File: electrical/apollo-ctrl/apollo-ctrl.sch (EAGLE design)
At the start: 24 parts, among them J1 BARREL-JACK, Q1 N-chan, U1 NANO

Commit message: DIY version of PCB sort of done, require review
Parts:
- removed J1: BARREL-JACK, apollo-ctrl:POWER_JACKPTH
- added BAT1: (no value), apollo-ctrl:BATTERYAA-KIT
- added C1: 47u or more, apollo-ctrl:CAP_POLPTH4
- added C2: 100n, apollo-ctrl:CAPPTH
- added COIL2: (no value), apollo-ctrl:M023.5MM
- added D10, D11, D12: 3V6, apollo-ctrl:DIODE-ZENER1N4148
- added D4, D5: DIODE-SCHOTTKYPTH, apollo-ctrl:DIODE-SCHOTTKYPTH
- added D6, D7, D8, D9: (no value), apollo-ctrl:DIODE1N4148
- added F3: PTC, apollo-ctrl:PTCPTH
- added JP7, JP8: STAND-OFF, apollo-ctrl:STAND-OFF
- added LOGO1: APOLLO-LOGO, apollo-ctrl:APOLLO-LOGO
- added OK2: PC817, apollo-ctrl:PC817
- added Q2: N-chan, apollo-ctrl:MOSFET-NCHANNELPTH2
- added R10, R11, R12, R13, R14, R15, R7, R8: 620R, apollo-ctrl:RESISTORPTH-1/4W
- added R6, R9: 10K, apollo-ctrl:RESISTORPTH-1/4W
- added S1: (no value), apollo-ctrl:TAC_SWITCHPTH
- added TVS3, TVS4, TVS5, TVS6, TVS7: TVS 16V, apollo-ctrl:TVS1N4148
- added U2: HONEYWELL-MPR, apollo-ctrl:HONEYWELL-MPR-GAGE-DIY
- added X1: BARREL-JACK, apollo-ctrl:POWER_JACKPTH
- added X2: SENSOR-O2, apollo-ctrl:SENSOR-O2-JST-VERT
- added X3: (no value), apollo-ctrl:M05PTH
- D1: value (none) -> 3V6; device apollo-ctrl:DIODE1N4148 -> apollo-ctrl:DIODE-ZENER1N4148
- D2: value (none) -> DIODE-SCHOTTKYPTH; device apollo-ctrl:DIODE1N4148 -> apollo-ctrl:DIODE-SCHOTTKYPTH
- F1: value PTC -> FUSE 3A; device apollo-ctrl:PTCPTH -> apollo-ctrl:FUSE-4PIN-KEYSTONE-3568; SKU RHEF070HF-ND -> (none)
- F2: value FUSE 3A -> PTC; device apollo-ctrl:FUSE-4PIN-KEYSTONE-3568 -> apollo-ctrl:PTCPTH; SKU (none) -> RHEF070HF-ND
- LED1: value (none) -> GRN
- LED2: value (none) -> RED
- R1: value 1K -> 470R 500mW; device apollo-ctrl:RESISTORPTH-1/4W -> apollo-ctrl:RESISTORPTH-1/2W
- R5: value 1K -> 4K7
- SG1: value BUZZER-POL-AI-3035 -> BUZZER
- TVS1: device apollo-ctrl:TVS -> apollo-ctrl:TVS1N4148; SKU P6KE16CALFCT-ND -> (none)
- TVS2: value TVS -> TVS 16V; device apollo-ctrl:TVS -> apollo-ctrl:TVS1N4148; SKU (none) -> P6KE16CALFCT-ND
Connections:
- removed net N$1: COIL1.2, D1.C, TVS2.2
- new net 3.3V: C2.1, R4.2, R5.2, U1.3.3V, U2.VDD
- new net 5V: D4.C, U1.5V, X2.VCC, X3.5
- new net AUX: U1.D12/MOSI, X3.2
- new net BUTTON: S1.1, S1.2, TVS5.C, U1.D11/MISO
- new net BUZZ: SG1.P, U1.D8/ICP1
- new net COIL-2: R10.1, R9.2, U1.D6/OC0A
- new net COIL-2-CHECK: OK2.COL, U1.D7
- new net LED-G: R12.2, U1.D10/OC1B
- new net LED-R: R13.2, U1.D9/OC1A
- new net MCU-TO-O2: R14.2, U1.D3/INT1/OC2B
- new net N$10: COIL2.1, D8.A, D9.A, F3.2, TVS4.C
- new net N$11: F3.1, Q2.D
- new net N$12: D9.C, R11.1
- new net N$13: D3.C, D5.A, F1.2A, F1.2B, R2.2
- new net N$14: BAT1.+, D2.C, D4.A
- new net N$15: LED2.A, R13.1
- new net N$16: LED1.A, R12.1
- new net N$17: R14.1, TVS6.C, X2.RX
- new net N$18: R15.1, TVS7.C, X2.TX
- new net N$19: D1.C, D2.A, R1.1
- new net N$8: OK2.A, R11.2
- new net N$9: Q2.G, R10.2
- new net O2-TO-MCU: R15.2, U1.D2/INT0
- new net SCL: D10.C, R4.1, U1.A5/SCL, U2.SCLK/SCL, X3.4
- new net SDA: D11.C, R5.1, U1.A4/SDA, U2.MOSI/SDA, X3.3
- net +12V: now also C1.+, COIL1.2, COIL2.2, D5.C, D6.C, D8.C, R1.2, TVS1.C, TVS3.C, U1.VBAT; no longer D3.C, F2.2A, F2.2B, R4.2
- net COIL-1: now also R6.2, R7.1, U1.D4; no longer R1.1, R2.2
- net COIL-1-CHECK: now also U1.D5/OC0B
- net GND: now also BAT1.-, C1.-, C2.2, D1.A, D10.A, D11.A, D12.A, LED1.C, LED2.C, OK2.C, OK2.EMIT, Q2.S, R3.1, R6.1, R9.1, S1.3, S1.4, SG1.N, TVS1.A, TVS2.A, TVS3.A, TVS4.A, TVS5.A, TVS6.A, TVS7.A, U1.GND, U1.GND2, U2.VSS, X1.GND, X1.GNDBREAK, X2.GND, X3.1; no longer J1.GND, J1.GNDBREAK, R2.1, R5.1, TVS1.1, TVS2.1
- net N$2: now also F2.1; no longer F1.1
- net N$3: now also R7.2; no longer R1.2
- net N$4: now also R8.2; no longer R3.2
- net N$5: now also D6.A, D7.A, F2.2, TVS2.C; no longer D1.A, D2.A, F1.2, TVS1.2
- net N$6: now also F1.1A, F1.1B, X1.PWR; no longer F2.1A, F2.1B, J1.PWR
- net N$7: now also D7.C, R8.1; no longer D2.C, R3.1
- net V-MON: now also D12.C, R2.1, R3.2, U1.A3; no longer R4.1, R5.2
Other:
- note added: "backup power diode-OR"
- note added: "continuity checker"
- note added: "detects if coil is open or fuse is blown"
- note added: "flyback"
- note added: "over-voltage and reverse polarity protection"
- note added: "poor-man's battery charger treats the battery like a super-cap use Li-Ion only! 14400 cell"
- note added: "power fail detection"
- moved on the sheet: COIL1, D3, F1, F2, LED1, LED2, OK1, Q1, R1, R2, R3, R4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

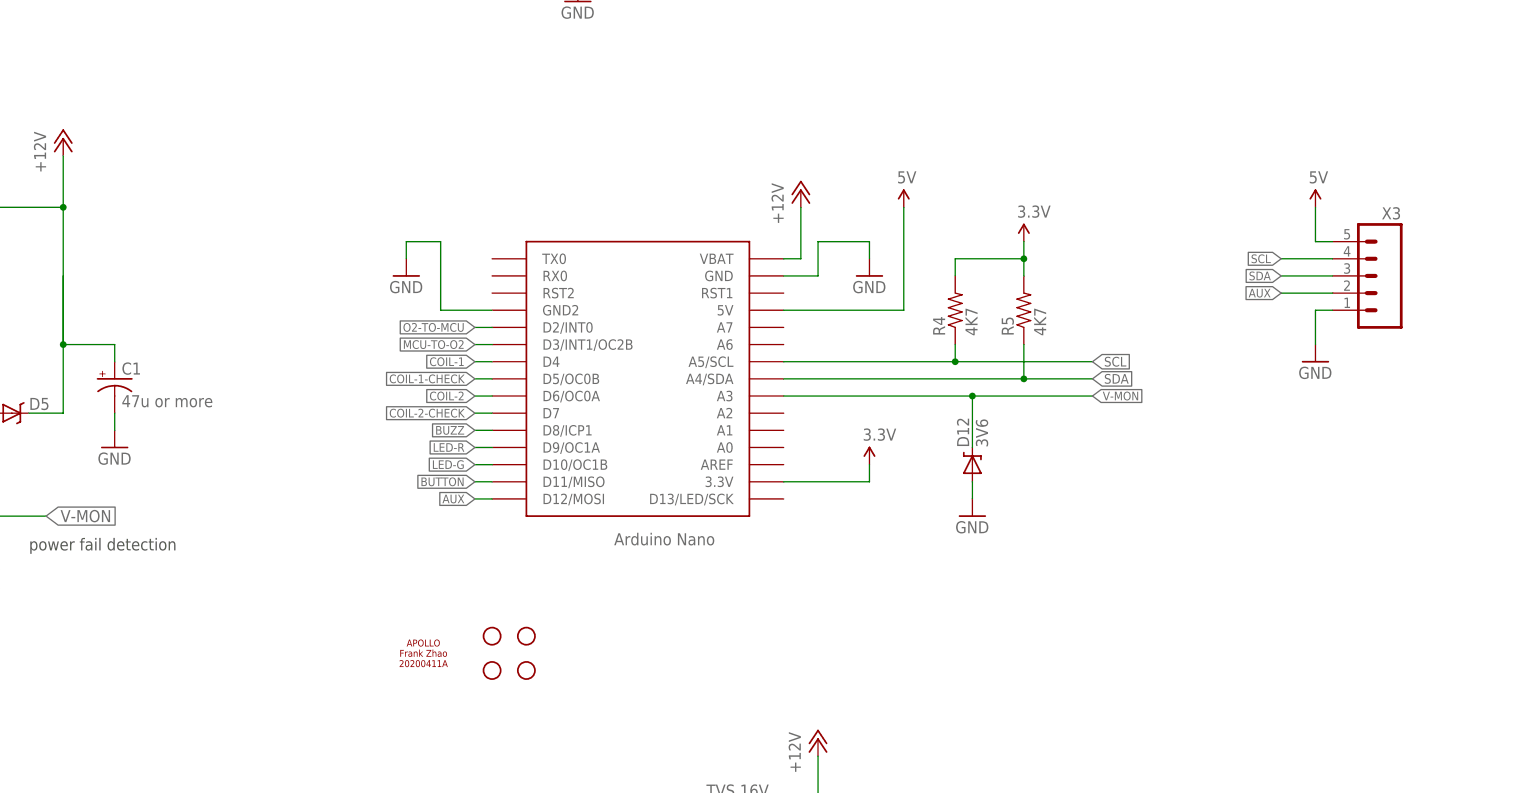
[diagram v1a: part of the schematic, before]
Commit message: added more spare pins to i2c header
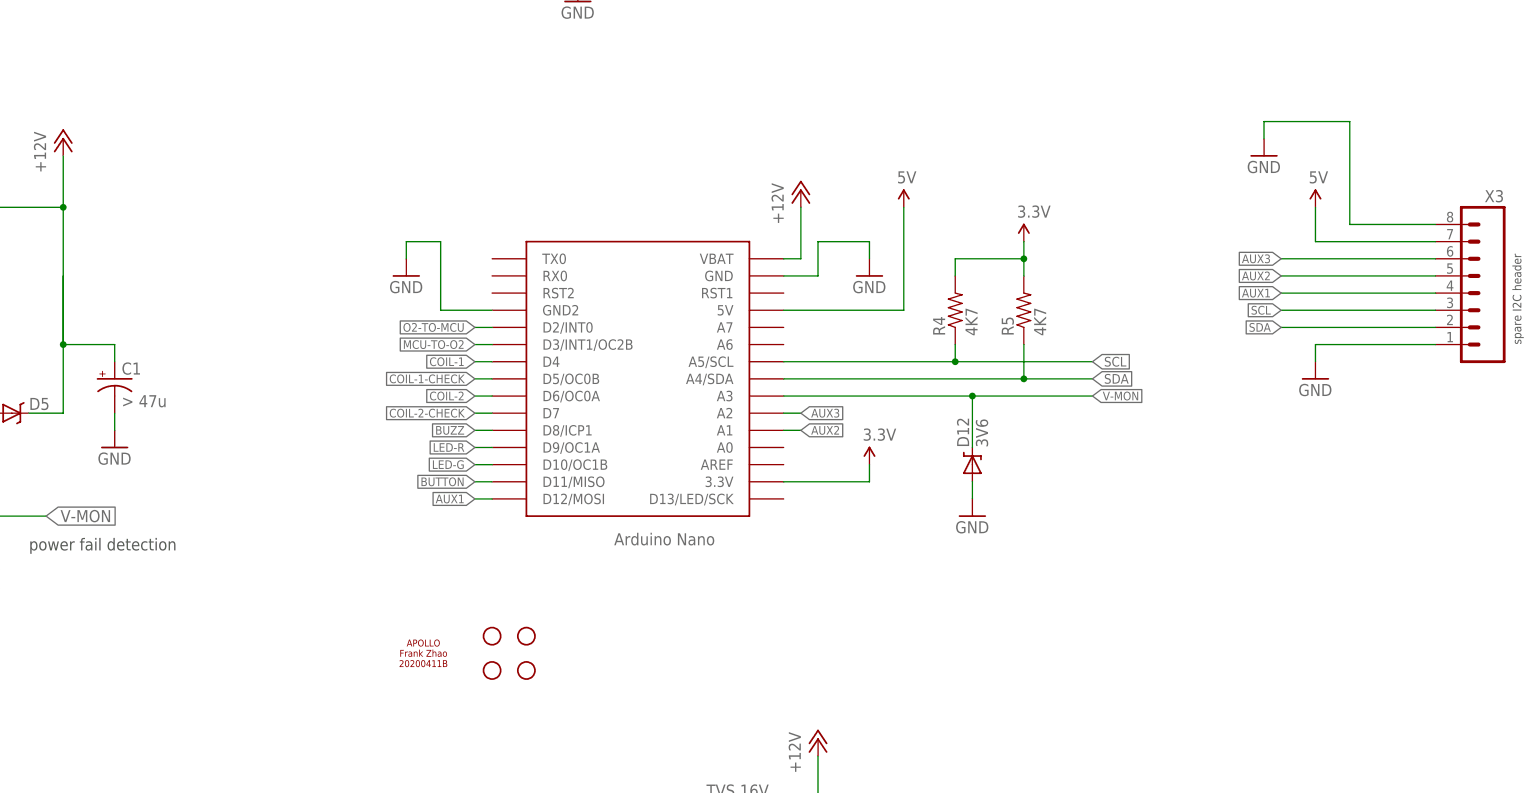
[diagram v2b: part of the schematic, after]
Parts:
- C1: value 47u or more -> > 47u
- X3: device apollo-ctrl:M05PTH -> apollo-ctrl:M081X08
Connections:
- removed net AUX: U1.D12/MOSI, X3.2
- new net AUX1: U1.D12/MOSI, X3.4
- new net AUX2: U1.A1, X3.5
- new net AUX3: U1.A2, X3.6
- net 5V: now also X3.7; no longer X3.5
- net GND: now also X3.8
- net SCL: now also X3.3; no longer X3.4
- net SDA: now also X3.2; no longer X3.3
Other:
- note added: "spare I2C header"
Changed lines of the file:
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@@
 <part name="C2" library="apollo-ctrl" deviceset="CAP" device="PTH" value="100n"/>
 <part name="GND5" library="apollo-ctrl" deviceset="GND" device=""/>
-<part name="C1" library="apollo-ctrl" deviceset="CAP_POL" device="PTH4" value="47u or more"/>
+<part name="C1" library="apollo-ctrl" deviceset="CAP_POL" device="PTH4" value="&gt; 47u"/>
 <part name="X2" library="apollo-ctrl" deviceset="SENSOR-O2" device="-JST-VERT" value="SENSOR-O2"/>
 <part name="GND26" library="apollo-ctrl" deviceset="GND" device=""/>
@@
 <part name="GND29" library="apollo-ctrl" deviceset="GND" device=""/>
 <part name="P+10" library="apollo-ctrl" deviceset="5V" device=""/>
-<part name="X3" library="apollo-ctrl" deviceset="M05" device="PTH"/>
 <part name="GND30" library="apollo-ctrl" deviceset="GND" device=""/>
 <part name="P+11" library="apollo-ctrl" deviceset="5V" device=""/>
+<part name="GND31" library="apollo-ctrl" deviceset="GND" device=""/>
+<part name="X3" library="apollo-ctrl" deviceset="M08" device="1X08"/>
 </parts>
 <sheets>
@@
 coil is open
 or fuse is blown</text>
+<text x="162.56" y="45.72" size="1.27" layer="97" rot="R90">spare I2C header</text>
 </plain>
 <instances>
@@
 <attribute name="VALUE" x="-87.376" y="56.896" size="1.778" layer="96"/>
 </instance>
-<instance part="X3" gate="G$1" x="142.24" y="55.88" rot="MR0"/>
-<instance part="GND30" gate="1" x="132.08" y="43.18" smashed="yes">
-<attribute name="VALUE" x="129.54" y="40.64" size="1.778" layer="96"/>
+<instance part="GND30" gate="1" x="132.08" y="40.64" smashed="yes">
+<attribute name="VALUE" x="129.54" y="38.1" size="1.778" layer="96"/>
 </instance>
 <instance part="P+11" gate="G$1" x="132.08" y="66.04" smashed="yes">
 <attribute name="VALUE" x="131.064" y="69.596" size="1.778" layer="96"/>
 </instance>
+<instance part="GND31" gate="1" x="124.46" y="73.66" smashed="yes">
+<attribute name="VALUE" x="121.92" y="71.12" size="1.778" layer="96"/>
+</instance>
+<instance part="X3" gate="G$1" x="154.94" y="53.34" rot="MR0"/>
 </instances>
 <busses>
@@
 <segment>
 <pinref part="GND30" gate="1" pin="GND"/>
-<wire x1="132.08" y1="45.72" x2="132.08" y2="50.8" width="0.1524" layer="91"/>
+<wire x1="132.08" y1="45.72" x2="132.08" y2="43.18" width="0.1524" layer="91"/>
+<wire x1="132.08" y1="45.72" x2="149.86" y2="45.72" width="0.1524" layer="91"/>
 <pinref part="X3" gate="G$1" pin="1"/>
-<wire x1="132.08" y1="50.8" x2="134.62" y2="50.8" width="0.1524" layer="91"/>
+</segment>
+<segment>
+<pinref part="GND31" gate="1" pin="GND"/>
+<wire x1="124.46" y1="76.2" x2="124.46" y2="78.74" width="0.1524" layer="91"/>
+<wire x1="124.46" y1="78.74" x2="137.16" y2="78.74" width="0.1524" layer="91"/>
+<wire x1="137.16" y1="78.74" x2="137.16" y2="63.5" width="0.1524" layer="91"/>
+<pinref part="X3" gate="G$1" pin="8"/>
+<wire x1="137.16" y1="63.5" x2="149.86" y2="63.5" width="0.1524" layer="91"/>
 </segment>
 </net>
@@
 </segment>
 <segment>
-<pinref part="X3" gate="G$1" pin="4"/>
-<wire x1="134.62" y1="58.42" x2="127" y2="58.42" width="0.1524" layer="91"/>
-<label x="127" y="58.42" size="1.27" layer="95" rot="R180" xref="yes"/>
+<label x="127" y="50.8" size="1.27" layer="95" rot="R180" xref="yes"/>
+<wire x1="127" y1="50.8" x2="149.86" y2="50.8" width="0.1524" layer="91"/>
+<pinref part="X3" gate="G$1" pin="3"/>
 </segment>
 </net>
@@
 </segment>
 <segment>
-<pinref part="X3" gate="G$1" pin="3"/>
-<wire x1="134.62" y1="55.88" x2="127" y2="55.88" width="0.1524" layer="91"/>
-<label x="127" y="55.88" size="1.27" layer="95" rot="R180" xref="yes"/>
+<label x="127" y="48.26" size="1.27" layer="95" rot="R180" xref="yes"/>
+<wire x1="127" y1="48.26" x2="149.86" y2="48.26" width="0.1524" layer="91"/>
+<pinref part="X3" gate="G$1" pin="2"/>
 </segment>
 </net>
@@
 </segment>
 <segment>
-<pinref part="X3" gate="G$1" pin="5"/>
 <pinref part="P+11" gate="G$1" pin="5V"/>
-<wire x1="134.62" y1="60.96" x2="132.08" y2="60.96" width="0.1524" layer="91"/>
 <wire x1="132.08" y1="60.96" x2="132.08" y2="66.04" width="0.1524" layer="91"/>
+<wire x1="149.86" y1="60.96" x2="132.08" y2="60.96" width="0.1524" layer="91"/>
+<pinref part="X3" gate="G$1" pin="7"/>
 </segment>
 </net>
@@
 </segment>
 </net>
-<net name="AUX" class="0">
-<segment>
-<pinref part="X3" gate="G$1" pin="2"/>
-<wire x1="134.62" y1="53.34" x2="127" y2="53.34" width="0.1524" layer="91"/>
+<net name="AUX2" class="0">
+<segment>
+<label x="127" y="55.88" size="1.27" layer="95" rot="R180" xref="yes"/>
+<wire x1="127" y1="55.88" x2="149.86" y2="55.88" width="0.1524" layer="91"/>
+<pinref part="X3" gate="G$1" pin="5"/>
+</segment>
+<segment>
+<pinref part="U1" gate="G$1" pin="A1"/>
+<wire x1="53.34" y1="33.02" x2="55.88" y2="33.02" width="0.1524" layer="91"/>
+<label x="55.88" y="33.02" size="1.27" layer="95" xref="yes"/>
+</segment>
+</net>
+<net name="AUX1" class="0">
+<segment>
 <label x="127" y="53.34" size="1.27" layer="95" rot="R180" xref="yes"/>
+<wire x1="127" y1="53.34" x2="149.86" y2="53.34" width="0.1524" layer="91"/>
+<pinref part="X3" gate="G$1" pin="4"/>
 </segment>
 <segment>
@@
 </segment>
 </net>
+<net name="AUX3" class="0">
+<segment>
+<label x="127" y="58.42" size="1.27" layer="95" rot="R180" xref="yes"/>
+<wire x1="127" y1="58.42" x2="149.86" y2="58.42" width="0.1524" layer="91"/>
+<pinref part="X3" gate="G$1" pin="6"/>
+</segment>
+<segment>
+<pinref part="U1" gate="G$1" pin="A2"/>
+<wire x1="53.34" y1="35.56" x2="55.88" y2="35.56" width="0.1524" layer="91"/>
+<label x="55.88" y="35.56" size="1.27" layer="95" xref="yes"/>
+</segment>
+</net>

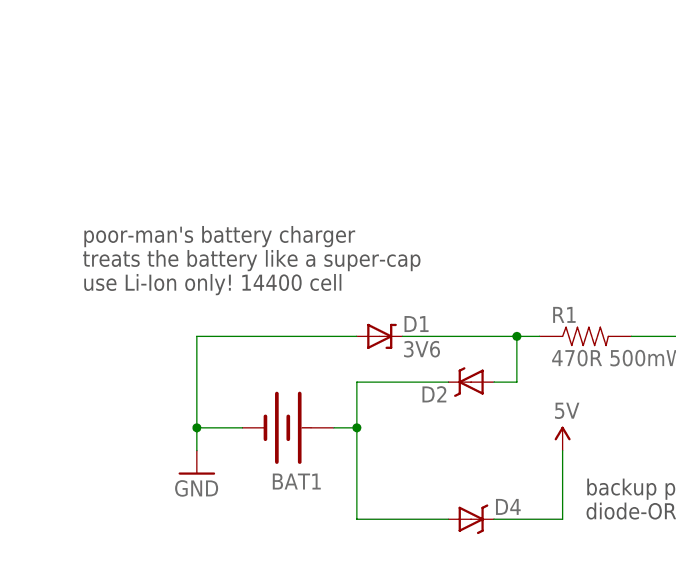
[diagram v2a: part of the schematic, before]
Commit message: fixed wrong battery type
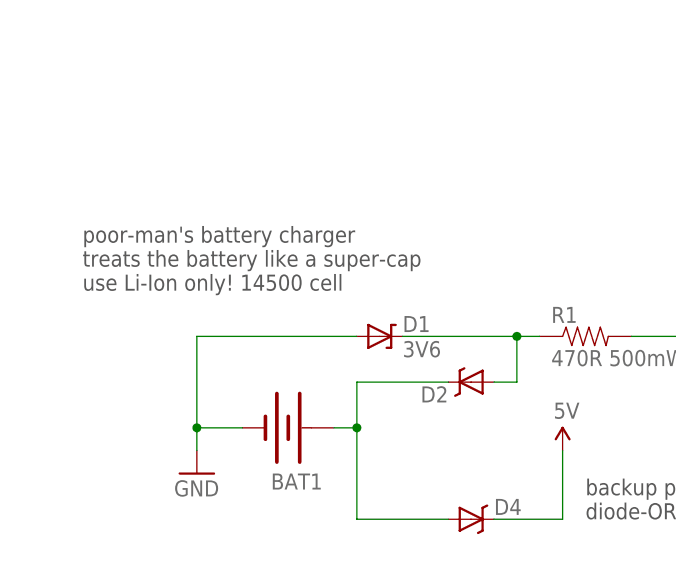
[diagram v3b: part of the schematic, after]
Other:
- note added: "poor-man's battery charger treats the battery like a super-cap use Li-Ion only! 14500 cell"
- note removed: "poor-man's battery charger treats the battery like a super-cap use Li-Ion only! 14400 cell"
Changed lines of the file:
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@@
 <text x="-139.7" y="71.12" size="1.778" layer="97">poor-man's battery charger
 treats the battery like a super-cap
-use Li-Ion only! 14400 cell</text>
+use Li-Ion only! 14500 cell</text>
 <text x="-53.34" y="-48.26" size="1.778" layer="97">continuity checker</text>
 <text x="-58.42" y="15.24" size="1.778" layer="97">power fail detection</text>
